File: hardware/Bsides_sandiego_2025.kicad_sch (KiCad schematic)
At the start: 23 parts, among them J1 Conn_02x03_Odd_Even, SW1 RESET, SW2 SW_SPDT, U1 CH32V003FxPx

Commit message: feat(Hw):Update_PCB_And_Floorplan
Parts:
- added C3, C4, C5, C6: 0.1uF, Capacitor_SMD:C_0603_1608Metric, symbol Device:C_Small
- added J2: OLED, Footprints:Display OLED 128 x32, symbol Connector:Screw_Terminal_01x04
- added SW3, SW4, SW5, SW6: ~, Button_Switch_SMD:SW_SPST_TL3342, symbol Switch:SW_Push
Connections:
- net GND: now also C3.1, C4.1, C5.1, C6.1, J2.4 (Pin_4), SW3.1, SW4.1, SW5.1, SW6.1
- net SCL: now also J2.2 (Pin_2)
- net SDA: now also J2.1 (Pin_1)
- net VCC: now also J2.3 (Pin_3)
- net LED2: now reaches D2.2 (A)
- net LED2: now also U1.2 (PD5)
- net LED7: now reaches D7.2 (A)
- net LED7: now also U1.10 (PC0)
- net LED6: now reaches D6.2 (A)
- net LED6: now also U1.8 (PD0)
- net LED3: now reaches D3.2 (A)
- net LED3: now also U1.3 (PD6)
- net LED1: now reaches D1.2 (A)
- net LED1: now also U1.1 (PD4)
- net LED5: now reaches D5.2 (A)
- net LED5: now also U1.6 (PA2)
- net LED4: now reaches D4.2 (A)
- net LED4: now also U1.5 (PA1)
- net LED8: now reaches U1.13 (PC3)
- net LED8: now also D8.2 (A)
- net LEFT: now reaches U1.14 (PC4)
- net LEFT: now also C3.2, SW3.2
- net UP: now reaches U1.15 (PC5)
- net UP: now also C5.2, SW5.2
- net DOWN: now reaches U1.19 (PD2)
- net DOWN: now also C6.2, SW6.2
- net RIGHT: now reaches U1.20 (PD3)
- net RIGHT: now also C4.2, SW4.2
- no-connect marks 18 -> 6
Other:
- moved on the sheet: D1, D2, D3, D4, D5, D6, D7, D8, R1, R2, R3, R4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

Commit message: feat(Hw):Update_Route
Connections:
- net VCC is gone; now on net +3.3V: C1.2, J2.3 (Pin_3), U1.9 (VDD)
- net DOWN: now also U1.6 (PA2); no longer U1.19 (PD2)
- net LED1: now also U1.20 (PD3); no longer U1.1 (PD4)
- net LED3: now also U1.1 (PD4); no longer U1.3 (PD6)
- net LED5: now also U1.19 (PD2); no longer U1.6 (PA2)
- net LED6: now also U1.15 (PC5); no longer U1.8 (PD0)
- net LED8: now also U1.3 (PD6); no longer U1.13 (PC3)
- net LEFT: now also U1.13 (PC3); no longer U1.14 (PC4)
- net RIGHT: now also U1.8 (PD0); no longer U1.20 (PD3)
- net UP: now also U1.14 (PC4); no longer U1.15 (PC5)
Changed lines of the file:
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@@
 	(wire
 		(pts
-			(xy 222.758 132.842) (xy 222.758 133.35)
+			(xy 222.25 130.81) (xy 222.25 133.35)
 		)
 		(stroke
@@
 	(wire
 		(pts
-			(xy 222.758 133.35) (xy 231.14 133.35)
+			(xy 222.25 133.35) (xy 231.14 133.35)
 		)
 		(stroke
@@
 	(wire
 		(pts
-			(xy 60.96 25.146) (xy 60.96 26.67)
+			(xy 60.96 24.13) (xy 60.96 26.67)
 		)
 		(stroke
@@
 	)
 	(label "LED8"
-		(at 45.72 48.26 180)
+		(at 74.93 55.88 0)
 		(fields_autoplaced yes)
 		(effects
@@
 				(size 1.27 1.27)
 			)
-			(justify right bottom)
+			(justify left bottom)
 		)
 	)
 	(label "DOWN"
-		(at 74.93 45.72 0)
+		(at 74.93 66.04 0)
 		(fields_autoplaced yes)
 		(effects
@@
 	)
 	(label "LED3"
-		(at 74.93 55.88 0)
+		(at 74.93 50.8 0)
 		(fields_autoplaced yes)
 		(effects
@@
 	)
 	(label "LEFT"
-		(at 45.72 50.8 180)
+		(at 45.72 48.26 180)
 		(fields_autoplaced yes)
 		(effects
@@
 	)
 	(label "LED6"
-		(at 74.93 40.64 0)
+		(at 45.72 53.34 180)
 		(fields_autoplaced yes)
 		(effects
@@
 				(size 1.27 1.27)
 			)
-			(justify left bottom)
+			(justify right bottom)
 		)
 	)
@@
 	)
 	(label "UP"
-		(at 45.72 53.34 180)
+		(at 45.72 50.8 180)
 		(fields_autoplaced yes)
 		(effects
@@
 	)
 	(label "RIGHT"
-		(at 74.93 48.26 0)
+		(at 74.93 40.64 0)
 		(fields_autoplaced yes)
 		(effects
@@
 	)
 	(label "LED5"
-		(at 74.93 66.04 0)
+		(at 74.93 45.72 0)
 		(fields_autoplaced yes)
 		(effects
@@
 	)
 	(label "LED1"
-		(at 74.93 50.8 0)
+		(at 74.93 48.26 0)
 		(fields_autoplaced yes)
 		(effects
@@
 	)
 	(symbol
-		(lib_id "power:VCC")
-		(at 60.96 25.146 0)
-		(unit 1)
-		(exclude_from_sim no)
-		(in_bom yes)
-		(on_board yes)
-		(dnp no)
-		(fields_autoplaced yes)
-		(property "Reference" "#PWR01"
-			(at 60.96 28.956 0)
-			(effects
-				(font
-					(size 1.27 1.27)
-				)
-				(hide yes)
-			)
-		)
-		(property "Value" "VCC"
-			(at 60.96 19.812 0)
-			(effects
-				(font
-					(size 1.27 1.27)
-				)
-			)
-		)
-		(property "Footprint" ""
-			(at 60.96 25.146 0)
-			(effects
-				(font
-					(size 1.27 1.27)
-				)
-				(hide yes)
-			)
-		)
-		(property "Datasheet" ""
-			(at 60.96 25.146 0)
-			(effects
-				(font
-					(size 1.27 1.27)
-				)
-				(hide yes)
-			)
-		)
-		(property "Description" "Power symbol creates a global label with name \"VCC\""
-			(at 60.96 25.146 0)
-			(effects
-				(font
-					(size 1.27 1.27)
-				)
-				(hide yes)
-			)
-		)
-		(pin "1"
-		)
-		(instances
-			(project "Bsides_sandiego_2025"
-				(path "/f17b11f7-cf2d-4178-8d8d-fa3b03b7f629"
-					(reference "#PWR01")
-					(unit 1)
-				)
-			)
-		)
-	)
-	(symbol
 		(lib_id "power:GND")
 		(at 148.844 140.208 0)
@@
 	)
 	(symbol
+		(lib_id "power:+3.3V")
+		(at 60.96 24.13 0)
+		(unit 1)
+		(exclude_from_sim no)
+		(in_bom yes)
+		(on_board yes)
+		(dnp no)
+		(fields_autoplaced yes)
+		(property "Reference" "#PWR01"
+			(at 60.96 27.94 0)
+			(effects
+				(font
+					(size 1.27 1.27)
+				)
+				(hide yes)
+			)
+		)
+		(property "Value" "+3.3V"
+			(at 60.96 19.177 0)
+			(effects
+				(font
+					(size 1.27 1.27)
+				)
+			)
+		)
+		(property "Footprint" ""
+			(at 60.96 24.13 0)
+			(effects
+				(font
+					(size 1.27 1.27)
+				)
+				(hide yes)
+			)
+		)
+		(property "Datasheet" ""
+			(at 60.96 24.13 0)
+			(effects
+				(font
+					(size 1.27 1.27)
+				)
+				(hide yes)
+			)
+		)
+		(property "Description" ""
+			(at 60.96 24.13 0)
+			(effects
+				(font
+					(size 1.27 1.27)
+				)
+				(hide yes)
+			)
+		)
+		(pin "1"
+		)
+		(instances
+			(project "Bsides_sandiego_2025"
+				(path "/f17b11f7-cf2d-4178-8d8d-fa3b03b7f629"
+					(reference "#PWR01")
+					(unit 1)
+				)
+			)
+		)
+	)
+	(symbol
 		(lib_id "Switch:SW_Push")
 		(at 137.922 171.45 0)
@@
 	)
 	(symbol
+		(lib_id "power:+3.3V")
+		(at 222.25 130.81 0)
+		(unit 1)
+		(exclude_from_sim no)
+		(in_bom yes)
+		(on_board yes)
+		(dnp no)
+		(fields_autoplaced yes)
+		(property "Reference" "#PWR015"
+			(at 222.25 134.62 0)
+			(effects
+				(font
+					(size 1.27 1.27)
+				)
+				(hide yes)
+			)
+		)
+		(property "Value" "+3.3V"
+			(at 222.25 125.857 0)
+			(effects
+				(font
+					(size 1.27 1.27)
+				)
+			)
+		)
+		(property "Footprint" ""
+			(at 222.25 130.81 0)
+			(effects
+				(font
+					(size 1.27 1.27)
+				)
+				(hide yes)
+			)
+		)
+		(property "Datasheet" ""
+			(at 222.25 130.81 0)
+			(effects
+				(font
+					(size 1.27 1.27)
+				)
+				(hide yes)
+			)
+		)
+		(property "Description" ""
+			(at 222.25 130.81 0)
+			(effects
+				(font
+					(size 1.27 1.27)
+				)
+				(hide yes)
+			)
+		)
+		(pin "1"
+		)
+		(instances
+			(project "Bsides_sandiego_2025"
+				(path "/f17b11f7-cf2d-4178-8d8d-fa3b03b7f629"
+					(reference "#PWR015")
+					(unit 1)
+				)
+			)
+		)
+	)
+	(symbol
 		(lib_id "Switch:SW_Push")
 		(at 139.7 116.84 0)
@@
 					(unit 1)
 				)
-			)
-		)
-	)
-	(symbol
-		(lib_id "power:VCC")
-		(at 222.758 132.842 0)
-		(unit 1)
-		(exclude_from_sim no)
-		(in_bom yes)
-		(on_board yes)
-		(dnp no)
-		(fields_autoplaced yes)
-		(property "Reference" "#PWR010"
-			(at 222.758 136.652 0)
-			(effects
-				(font
-					(size 1.27 1.27)
-				)
-				(hide yes)
-			)
-		)
-		(property "Value" "VCC"
-			(at 222.758 127.508 0)
-			(effects
-				(font
-					(size 1.27 1.27)
-				)
-			)
-		)
-		(property "Footprint" ""
-			(at 222.758 132.842 0)
-			(effects
-				(font
-					(size 1.27 1.27)
-				)
-				(hide yes)
-			)
-		)
-		(property "Datasheet" ""
-			(at 222.758 132.842 0)
-			(effects
-				(font
-					(size 1.27 1.27)
-				)
-				(hide yes)
-			)
-		)
-		(property "Description" "Power symbol creates a global label with name \"VCC\""
-			(at 222.758 132.842 0)
-			(effects
-				(font
-					(size 1.27 1.27)
-				)
-				(hide yes)
-			)
-		)
-		(pin "1"
-		)
-		(instances
-			(project "Bsides_sandiego_2025"
-				(path "/f17b11f7-cf2d-4178-8d8d-fa3b03b7f629"
-					(reference "#PWR010")
-					(unit 1)
-				)

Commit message: feat(Hw):Update_BOM
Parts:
- D1: LCSC# (none) -> C5440628
- D2: LCSC# (none) -> C434450
- D3: LCSC# (none) -> C434424
- D8: LCSC# (none) -> C409795
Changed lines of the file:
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@@
 			)
 		)
+		(property "LCSC#" "C434450"
+			(at 50.8 125.73 0)
+			(effects
+				(font
+					(size 1.27 1.27)
+				)
+				(hide yes)
+			)
+		)
 		(pin "1"
 		)
@@
 			)
 		)
+		(property "LCSC#" "C434424"
+			(at 50.8 133.35 0)
+			(effects
+				(font
+					(size 1.27 1.27)
+				)
+				(hide yes)
+			)
+		)
 		(pin "1"
 		)
@@
 			)
 		)
+		(property "LCSC#" "C5440628"
+			(at 50.8 118.11 0)
+			(effects
+				(font
+					(size 1.27 1.27)
+				)
+				(hide yes)
+			)
+		)
 		(pin "1"
 		)
@@
 			(at 52.07 171.45 0)
 			(effects
+				(font
+					(size 1.27 1.27)
+				)
+				(hide yes)
+			)
+		)
+		(property "LCSC#" "C409795"
+			(at 52.07 171.45 0)
+			(effects

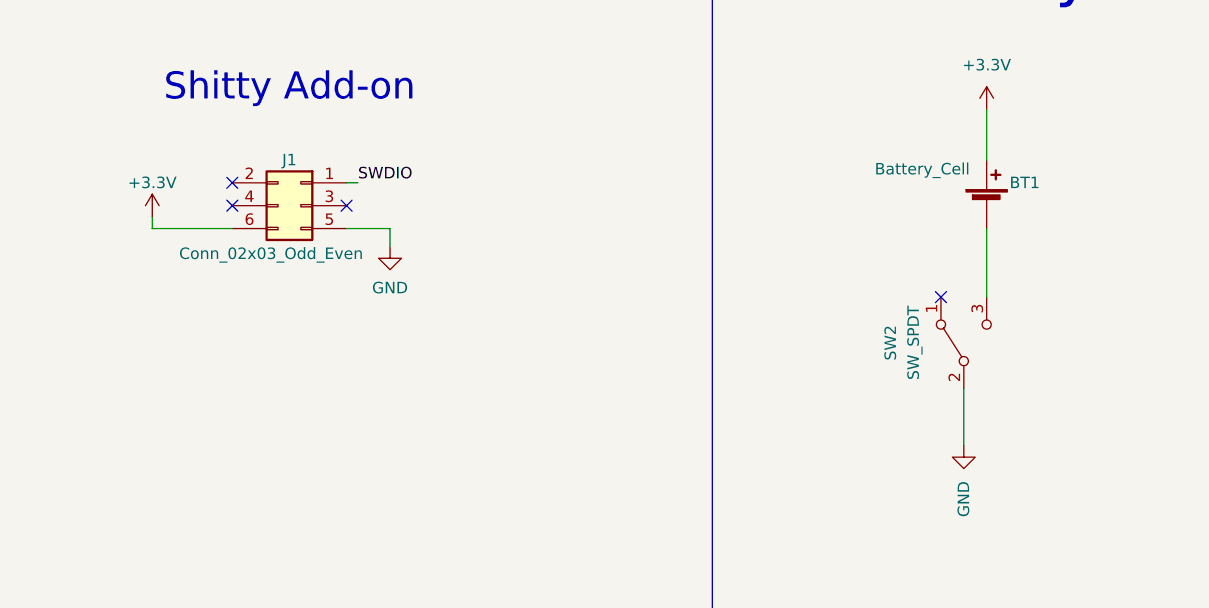
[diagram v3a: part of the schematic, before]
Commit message: feat(Hw):Update_Batt_Holder
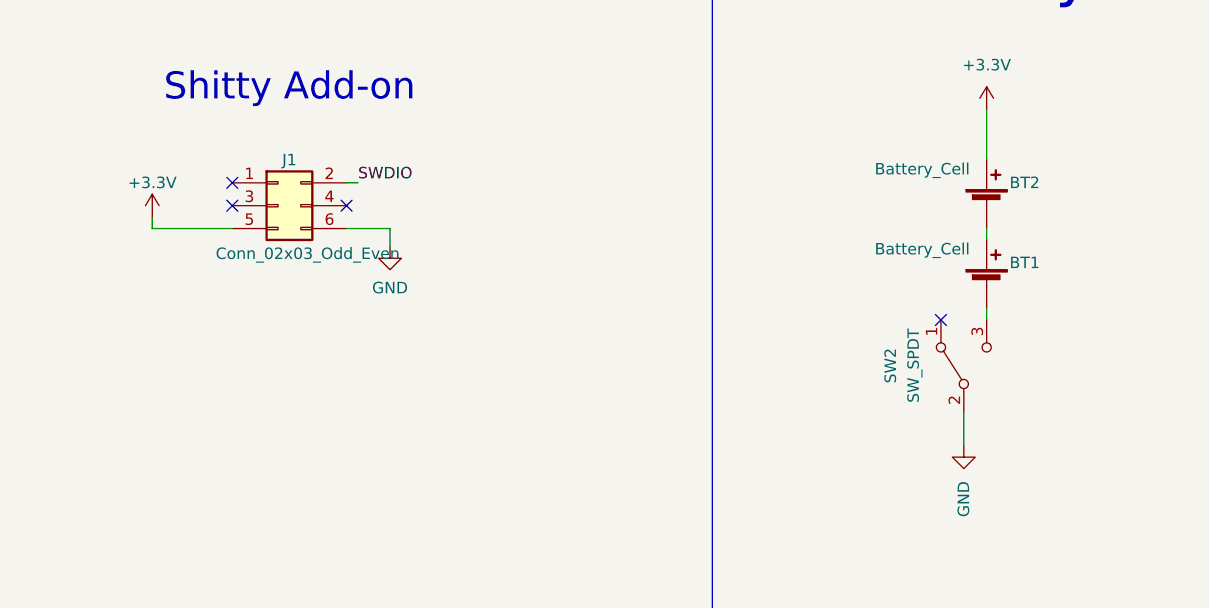
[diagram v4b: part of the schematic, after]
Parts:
- added BT2: Battery_Cell, Battery:BatteryHolder_Keystone_2466_1xAAA, symbol Device:Battery_Cell
- BT1: footprint Batteries:BAT-HLD-001 -> Battery:BatteryHolder_Keystone_2466_1xAAA
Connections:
- net +3.3V: now also J1.5 (Pin_5), BT2.2 (+); no longer BT1.2 (+), J1.6 (Pin_6)
- net GND: now also J1.6 (Pin_6); no longer J1.5 (Pin_5)
- net SWDIO: now also J1.2 (Pin_2); no longer J1.1 (Pin_1)
- new net: BT1.2 (+), BT2.1 (-)
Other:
- moved on the sheet: BT1, SW2
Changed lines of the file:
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@@
 	)
 	(no_connect
-		(at 252.73 60.96)
+		(at 252.73 63.5)
 	)
 	(no_connect
@@
 	(wire
 		(pts
-			(xy 257.81 40.132) (xy 257.81 45.72)
-		)
-		(stroke
-			(width 0)
-			(type default)
-		)
-	)
-	(wire
-		(pts
 			(xy 58.42 140.97) (xy 53.34 140.97)
 		)
@@
 	(wire
 		(pts
+			(xy 257.81 40.132) (xy 257.81 45.72)
+		)
+		(stroke
+			(width 0)
+			(type default)
+		)
+	)
+	(wire
+		(pts
 			(xy 165.1 53.34) (xy 173.99 53.34)
 		)
@@
 	(wire
 		(pts
+			(xy 257.81 54.61) (xy 257.81 53.34)
+		)
+		(stroke
+			(width 0)
+			(type default)
+		)
+	)
+	(wire
+		(pts
 			(xy 58.42 118.11) (xy 54.61 118.11)
 		)
@@
 	(wire
 		(pts
-			(xy 257.81 53.34) (xy 257.81 60.96)
+			(xy 43.18 125.73) (xy 46.99 125.73)
 		)
 		(stroke
@@
 	(wire
 		(pts
-			(xy 43.18 125.73) (xy 46.99 125.73)
+			(xy 135.636 155.956) (xy 132.334 155.956)
 		)
 		(stroke
@@
 	(wire
 		(pts
-			(xy 135.636 155.956) (xy 132.334 155.956)
+			(xy 257.81 63.5) (xy 257.81 62.23)
 		)
 		(stroke
@@
 	(wire
 		(pts
-			(xy 255.27 71.12) (xy 255.27 77.47)
+			(xy 255.27 73.66) (xy 255.27 77.47)
 		)
 		(stroke
@@
 	(wire
 		(pts
-			(xy 191.516 53.34) (xy 186.69 53.34)
+			(xy 191.516 55.372) (xy 191.516 53.34)
 		)
 		(stroke
@@
 	(wire
 		(pts
-			(xy 191.516 55.372) (xy 191.516 53.34)
+			(xy 186.69 53.34) (xy 191.516 53.34)
 		)
 		(stroke
@@
 	(symbol
 		(lib_id "Switch:SW_SPDT")
-		(at 255.27 66.04 90)
+		(at 255.27 68.58 90)
 		(unit 1)
 		(exclude_from_sim no)
@@
 		(dnp no)
 		(property "Reference" "SW2"
-			(at 247.142 66.04 0)
+			(at 247.142 68.58 0)
 			(effects
 				(font
@@
 		)
 		(property "Value" "SW_SPDT"
-			(at 249.682 66.04 0)
+			(at 249.682 68.58 0)
 			(effects
 				(font
@@
 		)
 		(property "Footprint" "Footprints:MSK12C02"
-			(at 255.27 66.04 0)
+			(at 255.27 68.58 0)
 			(effects
 				(font
@@
 		)
 		(property "Datasheet" "~"
-			(at 255.27 66.04 0)
+			(at 255.27 68.58 0)
 			(effects
 				(font
@@
 		)
 		(property "Description" ""
-			(at 255.27 66.04 0)
+			(at 255.27 68.58 0)
 			(effects
 				(font
@@
 		)
 		(property "LCSC#" "C431540"
-			(at 255.27 66.04 0)
+			(at 255.27 68.58 0)
 			(effects
 				(font
@@
 		)
 		(property "manf#" ""
-			(at 255.27 66.04 0)
+			(at 255.27 68.58 0)
 			(effects
 				(font
@@
 		)
 		(property "provedor" ""
-			(at 255.27 66.04 0)
+			(at 255.27 68.58 0)
 			(effects
 				(font
@@
 	(symbol
 		(lib_id "Device:Battery_Cell")
-		(at 257.81 50.8 0)
+		(at 257.81 59.69 0)
 		(unit 1)
 		(exclude_from_sim no)
@@
 		(dnp no)
 		(property "Reference" "BT1"
-			(at 260.35 48.26 0)
+			(at 260.35 57.15 0)
 			(effects
 				(font
@@
 		)
 		(property "Value" "Battery_Cell"
-			(at 245.364 46.736 0)
+			(at 245.364 55.626 0)
 			(effects
 				(font
@@
 			)
 		)
-		(property "Footprint" "Batteries:BAT-HLD-001"
-			(at 257.81 49.276 90)
+		(property "Footprint" "Battery:BatteryHolder_Keystone_2466_1xAAA"
+			(at 257.81 58.166 90)
 			(effects
 				(font
@@
 		)
 		(property "Datasheet" ""
-			(at 257.81 49.276 90)
+			(at 257.81 58.166 90)
 			(effects
 				(font
@@
 		)
 		(property "Description" ""
-			(at 257.81 50.8 0)
+			(at 257.81 59.69 0)
 			(effects
 				(font
@@
 		)
 		(property "LCSC#" "C964833"
-			(at 257.81 50.8 0)
+			(at 257.81 59.69 0)
 			(effects
 				(font
@@
 		)
 		(property "manf#" ""
-			(at 257.81 50.8 0)
+			(at 257.81 59.69 0)
 			(effects
 				(font
@@
 		)
 		(property "provedor" ""
-			(at 257.81 50.8 0)
+			(at 257.81 59.69 0)
 			(effects
 				(font
@@
 	)
 	(symbol
+		(lib_id "Device:Battery_Cell")
+		(at 257.81 50.8 0)
+		(unit 1)
+		(exclude_from_sim no)
+		(in_bom yes)
+		(on_board yes)
+		(dnp no)
+		(property "Reference" "BT2"
+			(at 260.35 48.26 0)
+			(effects
+				(font
+					(size 1.27 1.27)
+				)
+				(justify left)
+			)
+		)
+		(property "Value" "Battery_Cell"
+			(at 245.364 46.736 0)
+			(effects
+				(font
+					(size 1.27 1.27)
+				)
+				(justify left)
+			)
+		)
+		(property "Footprint" "Battery:BatteryHolder_Keystone_2466_1xAAA"
+			(at 257.81 49.276 90)
+			(effects
+				(font
+					(size 1.27 1.27)
+				)
+				(hide yes)
+			)
+		)
+		(property "Datasheet" ""
+			(at 257.81 49.276 90)
+			(effects
+				(font
+					(size 1.27 1.27)
+				)
+			)
+		)
+		(property "Description" ""
+			(at 257.81 50.8 0)
+			(effects
+				(font
+					(size 1.27 1.27)
+				)
+				(hide yes)
+			)
+		)
+		(property "LCSC#" "C964833"
+			(at 257.81 50.8 0)
+			(effects
+				(font
+					(size 1.27 1.27)
+				)
+				(hide yes)
+			)
+		)
+		(property "manf#" ""
+			(at 257.81 50.8 0)
+			(effects
+				(font
+					(size 1.27 1.27)
+				)
+				(hide yes)
+			)
+		)
+		(property "provedor" ""
+			(at 257.81 50.8 0)
+			(effects
+				(font
+					(size 1.27 1.27)
+				)
+				(hide yes)
+			)
+		)
+		(pin "2"
+		)
+		(pin "1"
+		)
+		(instances
+			(project "Bsides_sandiego_2025"
+				(path "/f17b11f7-cf2d-4178-8d8d-fa3b03b7f629"
+					(reference "BT2")
+					(unit 1)
+				)
+			)
+		)
+	)
+	(symbol
 		(lib_id "power:+3.3V")
 		(at 222.25 130.81 0)
@@
 	(symbol
 		(lib_id "Connector_Generic:Conn_02x03_Odd_Even")
-		(at 181.61 50.8 0)
-		(mirror y)
+		(at 179.07 50.8 0)
 		(unit 1)
 		(exclude_from_sim no)
@@
 		)
 		(property "Value" "Conn_02x03_Odd_Even"
-			(at 178.308 56.134 0)
+			(at 182.372 56.134 0)
 			(effects
 				(font
@@
 		)
 		(property "Footprint" "Connector_PinHeader_2.54mm:PinHeader_2x03_P2.54mm_Vertical_SMD"
-			(at 181.61 50.8 0)
+			(at 179.07 50.8 0)
 			(effects
 				(font
@@
 		)
 		(property "Datasheet" ""
-			(at 181.61 50.8 0)
+			(at 179.07 50.8 0)
 			(effects
 				(font
@@
 		)
 		(property "Description" ""
-			(at 181.61 50.8 0)
+			(at 179.07 50.8 0)
 			(effects
 				(font
@@
 		)
 		(property "LCSC#" "C124390"
-			(at 181.61 50.8 0)
+			(at 179.07 50.8 0)
 			(effects
 				(font
@@
 		)
 		(property "Proveedor" "JLCPCB"
-			(at 181.61 50.8 0)
+			(at 179.07 50.8 0)
 			(effects
 				(font
@@
 		)
 		(property "manf#" ""
-			(at 181.61 50.8 0)
+			(at 179.07 50.8 0)
 			(effects
 				(font
@@
 		)
 		(property "provedor" ""
-			(at 181.61 50.8 0)
+			(at 179.07 50.8 0)
 			(effects
 				(font

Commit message: feat(Hw):Update_csv_And_Size
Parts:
- BT1, BT2: LCSC# C964833 -> C5290189; manf# (none) -> BH-AAA-A1AJ001
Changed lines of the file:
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@@
 			)
 		)
-		(property "LCSC#" "C964833"
+		(property "LCSC#" "C5290189 "
 			(at 257.81 59.69 0)
 			(effects
@@
 			)
 		)
-		(property "manf#" ""
+		(property "manf#" "BH-AAA-A1AJ001 "
 			(at 257.81 59.69 0)
 			(effects
@@
 			)
 		)
-		(property "LCSC#" "C964833"
+		(property "LCSC#" "C5290189 "
 			(at 257.81 50.8 0)
 			(effects
@@
 			)
 		)
-		(property "manf#" ""
+		(property "manf#" "BH-AAA-A1AJ001 "
 			(at 257.81 50.8 0)
 			(effects

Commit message: feat(Hw):Update_Add_On_Connector
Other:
- company: (none) -> ElectronicCats
- title: (none) -> bsides-sandiego
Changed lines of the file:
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@@
 	(generator_version "8.0")
 	(paper "A4")
+	(title_block
+		(title "bsides-sandiego")
+		(date "2024-12-16")
+		(rev "v1.0")
+		(company "ElectronicCats")
+		(comment 1 "Lizeth Gallegos")
+		(comment 2 "Edgar Capuchino")
+	)
 	(junction
 		(at 31.75 171.45)

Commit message: fix(Hw):Update_J1_PartN.
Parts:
- J1: LCSC# C124390 -> C3975148
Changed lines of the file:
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@@
 			)
 		)
-		(property "LCSC#" "C124390"
+		(property "LCSC#" "C3975148"
 			(at 179.07 50.8 0)
 			(effects
